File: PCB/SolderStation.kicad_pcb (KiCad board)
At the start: 2 copper layers, 59.1 x 32.8 mm, 43 parts, among them J1 T12 TIP, J10 Aviation-GX12-6, J11 NTC, J2 DC IN, J3 ISP, J4 I2C, J5 Handset detect, J6 ENCODER, J7 OPTO, J8 LCD0802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

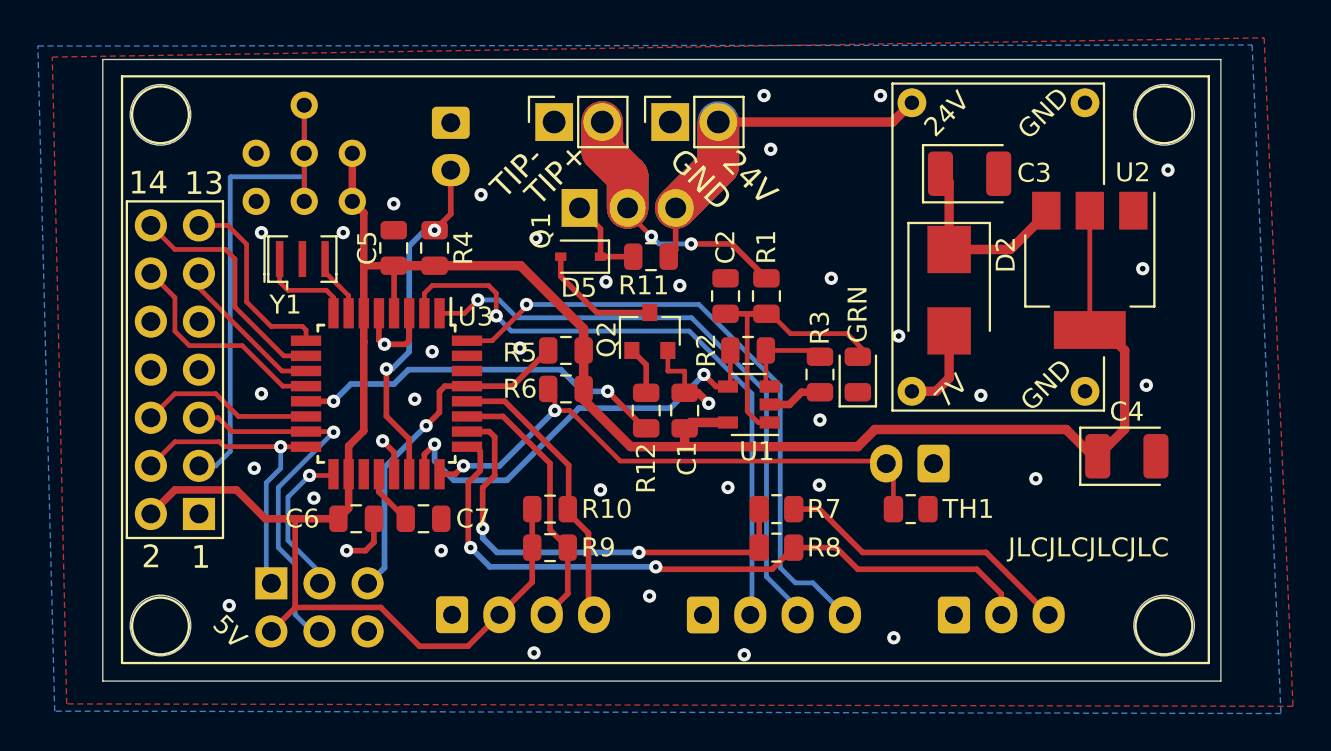
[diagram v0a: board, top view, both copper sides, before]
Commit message: Add files via upload
- Upgrade project to Kicad 7.0
- Improve schematic details
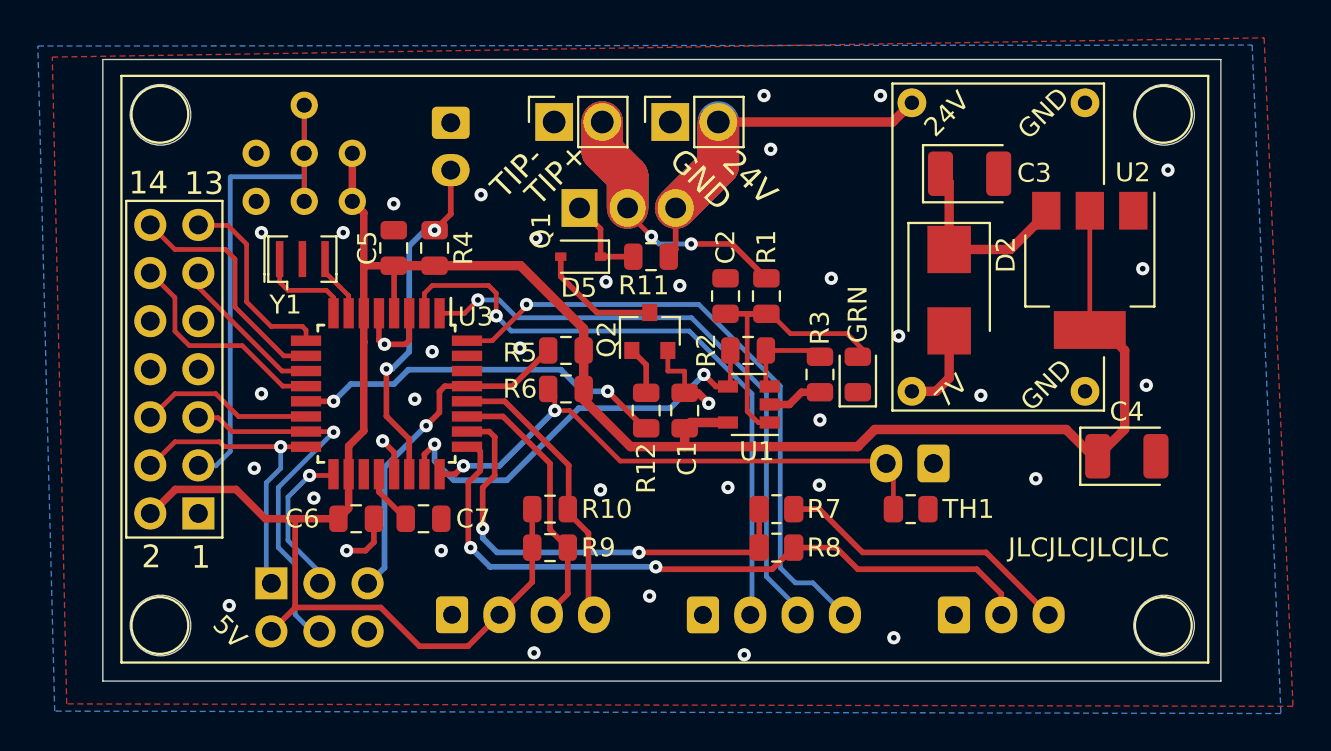
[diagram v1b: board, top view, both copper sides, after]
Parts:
- renumbered J8 to J12
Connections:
- net Net-(J7-Pad3) renamed /IR_PWR
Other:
- board text added: "T12.R05"
- board text removed: "T12.R04"
